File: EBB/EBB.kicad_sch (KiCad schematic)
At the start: 7 parts, among them J1 Conn_01x02, J3 Motor_Driver, J6 Motor, J7 Pi_Pico, J8 RFID_Module

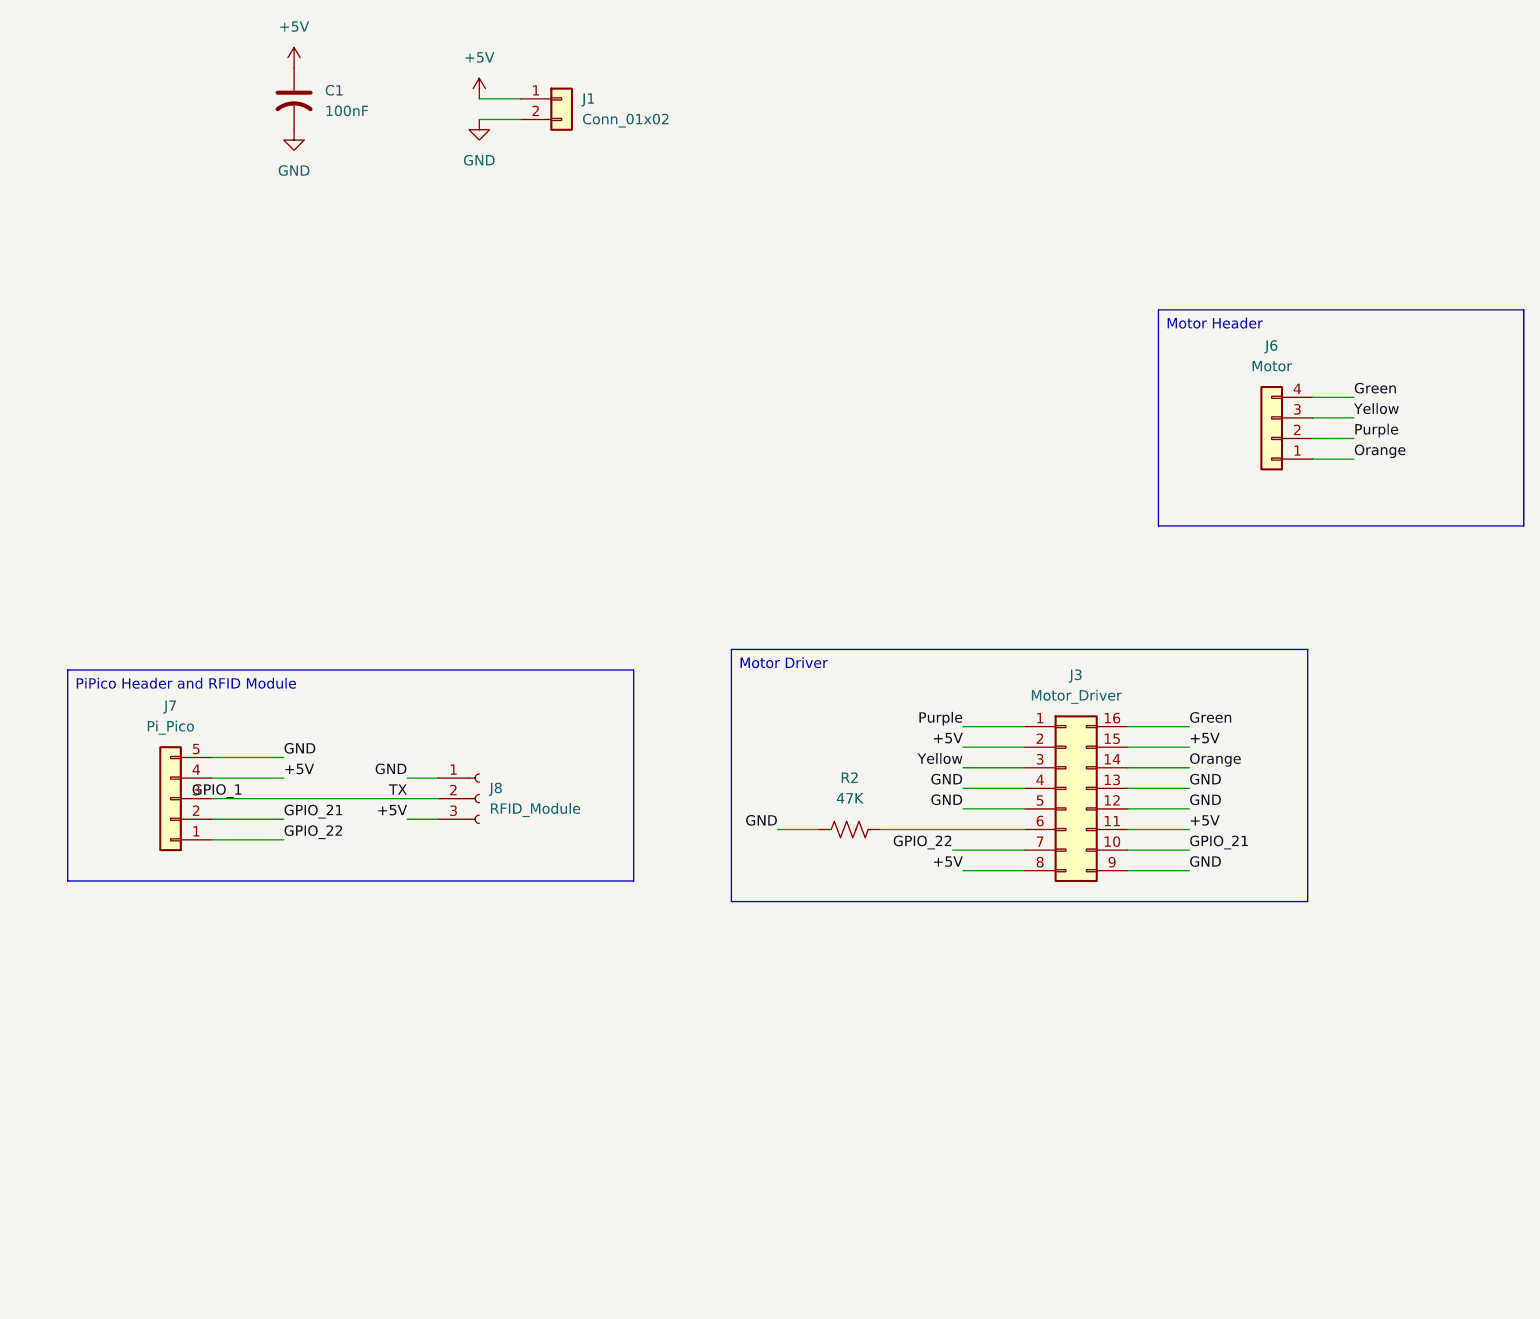
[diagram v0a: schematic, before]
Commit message: Updated KiCad files with pcb and footprints
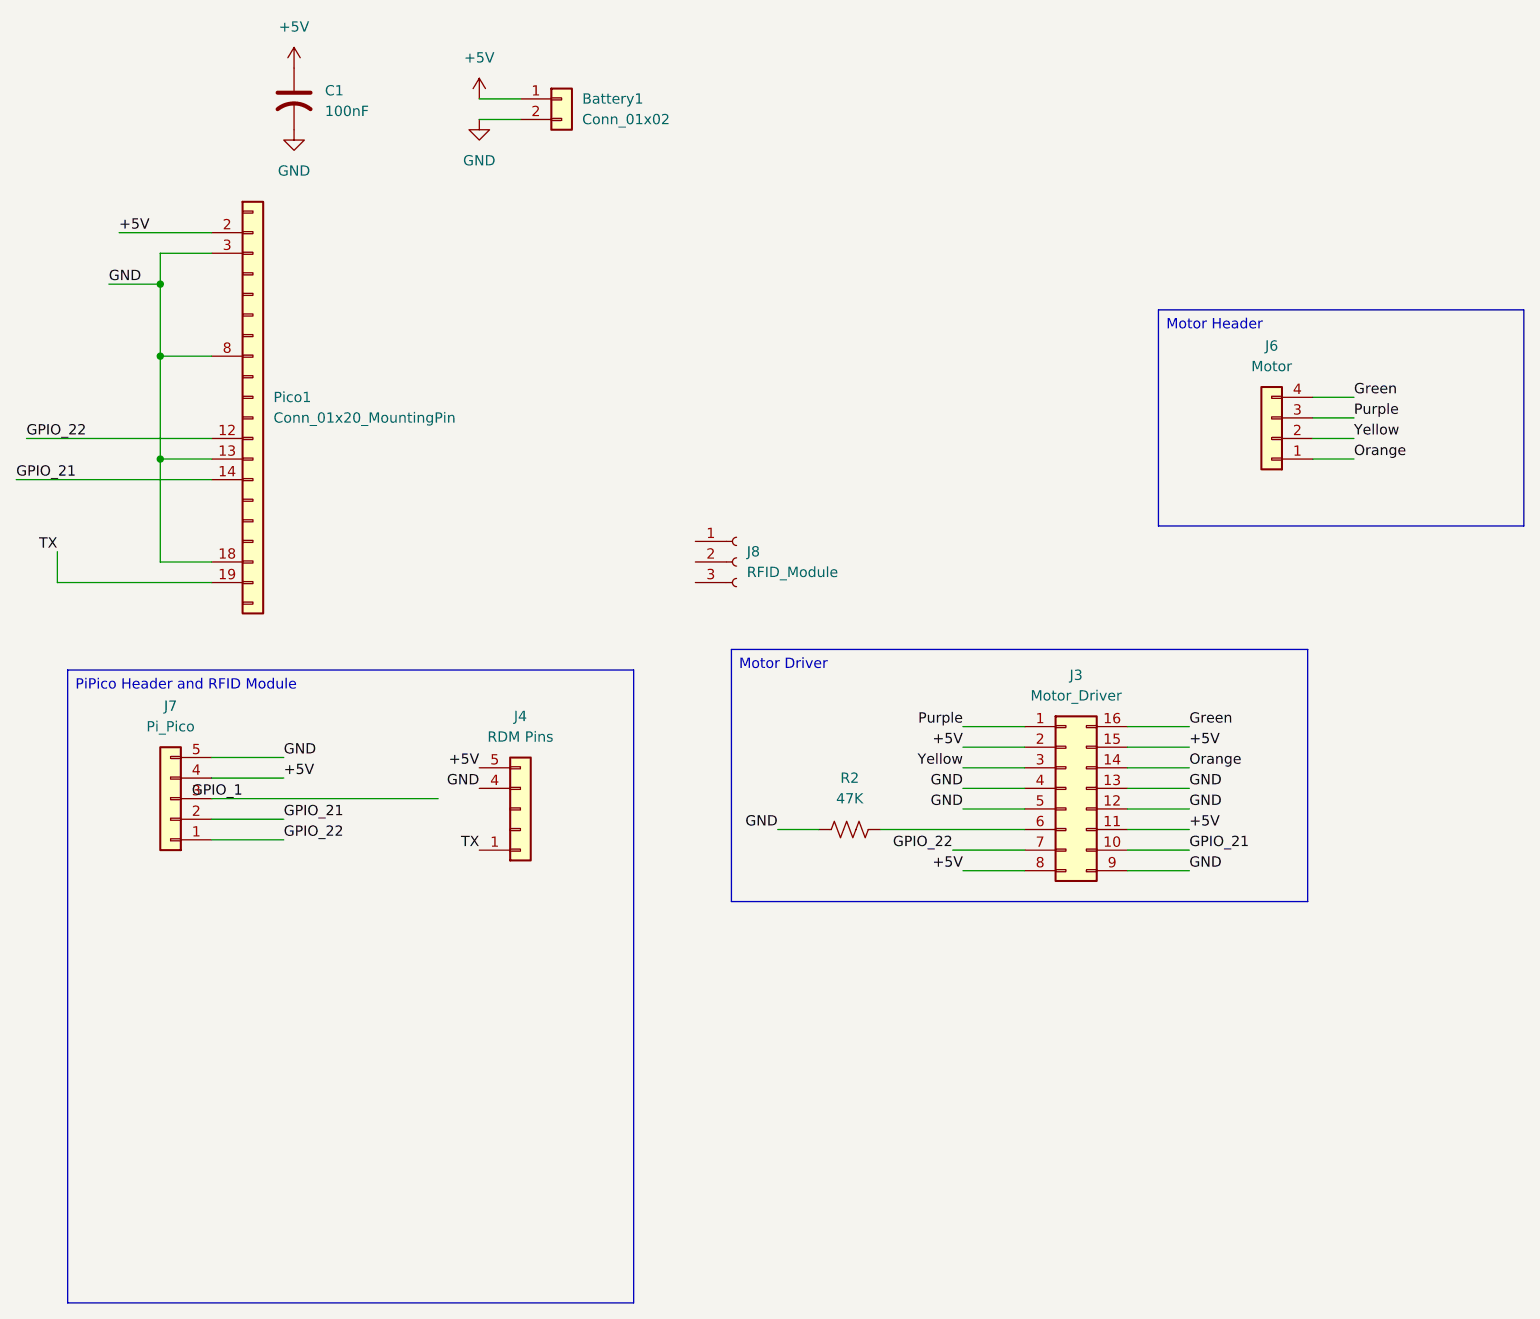
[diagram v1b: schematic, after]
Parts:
- added J4: RDM Pins, Connector_PinHeader_2.54mm:PinHeader_1x05_P2.54mm_Vertical, symbol Connector_Generic:Conn_01x05
- added Pico1: Conn_01x20_MountingPin, Connector_PinHeader_2.54mm:PinHeader_1x20_P2.54mm_Vertical, symbol Connector_Generic_MountingPin:Conn_01x20_MountingPin
- J7: footprint Connector_PinSocket_2.54mm:PinSocket_1x05_P2.54mm_Vertical -> (none)
- J8: footprint Connector_PinSocket_2.54mm:PinSocket_1x03_P2.54mm_Vertical -> (none)
- renumbered J1 to Battery1
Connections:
- net +5V: now also J4.5 (Pin_5), Pico1.2 (Pin_2); no longer J8.3 (Pin_3)
- net GND: now also J4.4 (Pin_4), Pico1.13 (Pin_13), Pico1.18 (Pin_18), Pico1.3 (Pin_3), Pico1.8 (Pin_8); no longer J8.1 (Pin_1)
- net GPIO_1: no longer J8.2 (Pin_2)
- net GPIO_21: now also Pico1.14 (Pin_14)
- net GPIO_22: now also Pico1.12 (Pin_12)
- net Purple: now also J6.3 (Pin_3); no longer J6.2 (Pin_2)
- net Yellow: now also J6.2 (Pin_2); no longer J6.3 (Pin_3)
- new net TX: J4.1 (Pin_1), Pico1.19 (Pin_19)
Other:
- moved on the sheet: J8
